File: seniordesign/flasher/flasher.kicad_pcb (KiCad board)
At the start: 2 copper layers, 17 parts, among them IC1 ATTINY24-SS, P1 PROG_PINS, P2 GPIO, P3 OUT, Q1 BC847S, Q2 BC847S

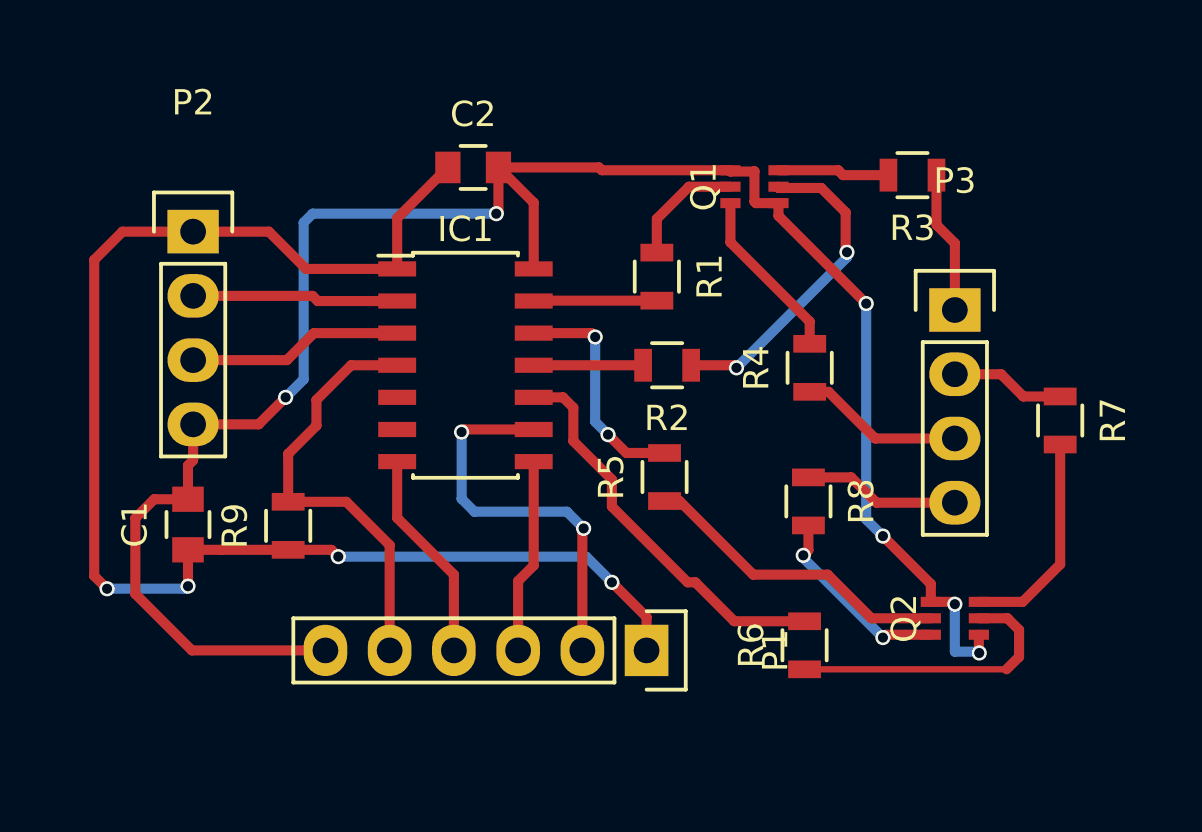
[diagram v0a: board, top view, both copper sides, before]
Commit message: Fix servo stuff, regenerate Gerber files for everything
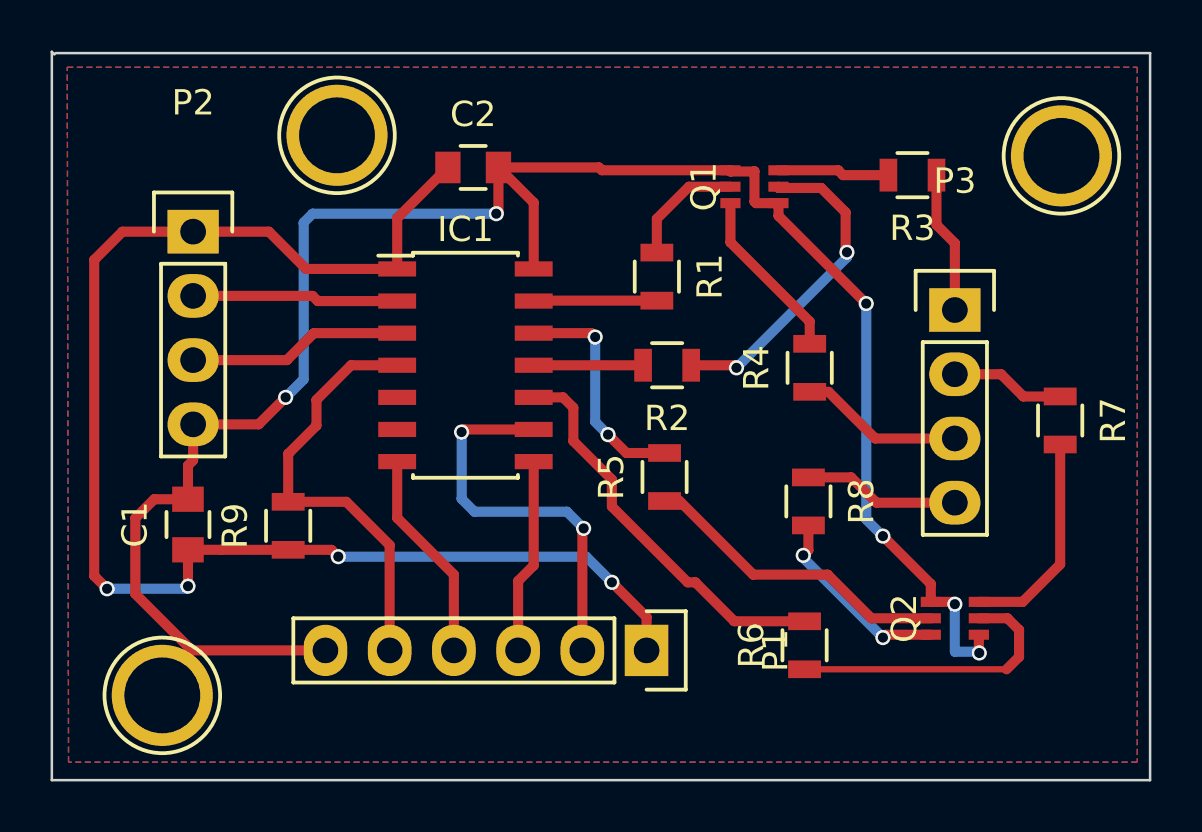
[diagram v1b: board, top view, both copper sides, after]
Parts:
- added REF**: 1pin, Connect:1pin, F.Cu at (144.3, 103.2)
- added REF**: 1pin, Connect:1pin, F.Cu at (179.9, 81.8)
- added REF**: 1pin, Connect:1pin, F.Cu at (151.2, 81.0)
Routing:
- added copper zone on B.Cu, net GND
- added copper zone on F.Cu, net GND
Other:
- board outline added: 43.4 x 28.8 mm
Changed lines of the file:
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@@
 (kicad_pcb (version 4) (host pcbnew "(2015-07-31 BZR 6030)-product")
   (general
-    (links 36)
+    (links 37)
     (no_connects 0)
-    (area 141.230399 78.611 183.183191 103.371801)
+    (area 139.903999 77.673999 183.438001 106.577601)
     (thickness 1.6)
-    (drawings 0)
+    (drawings 5)
     (tracks 175)
     (zones 0)
-    (modules 17)
+    (modules 20)
     (nets 27)
   )
@@
   )
   (setup
-    (last_trace_width 0.4)
+    (last_trace_width 0.25)
     (user_trace_width 0.4)
     (trace_clearance 0.2)
@@
     (mod_text_size 1 1)
     (mod_text_width 0.15)
-    (pad_size 1.5 1.5)
-    (pad_drill 0.6)
+    (pad_size 4 4)
+    (pad_drill 3)
     (pad_to_mask_clearance 0)
     (aux_axis_origin 0 0)
@@
       (outputformat 1)
       (mirror false)
-      (drillshape 1)
+      (drillshape 0)
       (scaleselection 1)
       (outputdirectory ""))
@@
     (add_net "Net-(Q2-Pad6)")
   )
+  (module Connect:1pin (layer F.Cu)
+    (at 144.3228 103.1748)
+    (descr "module 1 pin (ou trou mecanique de percage)")
+    (tags DEV)
+    (fp_text reference REF** (at 0 -3.048) (layer F.SilkS) hide
+      (effects (font (size 1 1) (thickness 0.15)))
+    )
+    (fp_text value 1pin (at 0 2.794) (layer F.Fab)
+      (effects (font (size 1 1) (thickness 0.15)))
+    )
+    (fp_circle (center 0 0) (end 0 -2.286) (layer F.SilkS) (width 0.15))
+    (pad 1 thru_hole circle (at 0 0) (size 4 4) (drill 3) (layers *.Cu *.Mask F.SilkS)
+      (net 2 GND))
+  )
+  (module Connect:1pin (layer F.Cu)
+    (at 179.8828 81.8388)
+    (descr "module 1 pin (ou trou mecanique de percage)")
+    (tags DEV)
+    (fp_text reference REF** (at 0 -3.048) (layer F.SilkS) hide
+      (effects (font (size 1 1) (thickness 0.15)))
+    )
+    (fp_text value 1pin (at 0 2.794) (layer F.Fab)
+      (effects (font (size 1 1) (thickness 0.15)))
+    )
+    (fp_circle (center 0 0) (end 0 -2.286) (layer F.SilkS) (width 0.15))
+    (pad 1 thru_hole circle (at 0 0) (size 4 4) (drill 3) (layers *.Cu *.Mask F.SilkS))
+  )
   (module Capacitors_SMD:C_0805 (layer F.Cu)
     (at 145.3388 96.4184 90)
@@
     )
   )
+  (module Connect:1pin (layer F.Cu)
+    (at 151.2316 81.026)
+    (descr "module 1 pin (ou trou mecanique de percage)")
+    (tags DEV)
+    (fp_text reference REF** (at 0 -3.048) (layer F.SilkS) hide
+      (effects (font (size 1 1) (thickness 0.15)))
+    )
+    (fp_text value 1pin (at 0 2.794) (layer F.Fab)
+      (effects (font (size 1 1) (thickness 0.15)))
+    )
+    (fp_circle (center 0 0) (end 0 -2.286) (layer F.SilkS) (width 0.15))
+    (pad 1 thru_hole circle (at 0 0) (size 4 4) (drill 3) (layers *.Cu *.Mask F.SilkS))
+  )
+  (gr_line (start 139.954 77.724) (end 140.0556 77.8256) (angle 90) (layer Edge.Cuts) (width 0.1))
+  (gr_line (start 139.954 106.5276) (end 139.954 77.724) (angle 90) (layer Edge.Cuts) (width 0.1))
+  (gr_line (start 183.388 106.5276) (end 139.954 106.5276) (angle 90) (layer Edge.Cuts) (width 0.1))
+  (gr_line (start 183.388 77.7748) (end 183.388 106.5276) (angle 90) (layer Edge.Cuts) (width 0.1))
+  (gr_line (start 140.1064 77.7748) (end 183.388 77.7748) (angle 90) (layer Edge.Cuts) (width 0.1))
   (segment (start 145.3388 97.4184) (end 145.3388 98.8568) (width 0.4) (layer F.Cu) (net 1))
   (segment (start 142.748 84.836) (end 145.542 84.836) (width 0.4) (layer F.Cu) (net 1))
@@
   (segment (start 159.0116 98.0364) (end 159.0116 93.9292) (width 0.4) (layer F.Cu) (net 9))
   (segment (start 158.3944 98.6536) (end 159.0116 98.0364) (width 0.4) (layer F.Cu) (net 9))
-  (segment (start 160.9344 101.3968) (end 160.9344 96.6216) (width 0.4) (layer F.Cu) (net 10) (status 400000))
-  (segment (start 156.2608 92.6592) (end 159.0116 92.6592) (width 0.4) (layer F.Cu) (net 10) (status 800000))
+  (segment (start 160.9344 101.3968) (end 160.9344 96.6216) (width 0.4) (layer F.Cu) (net 10))
+  (segment (start 156.2608 92.6592) (end 159.0116 92.6592) (width 0.4) (layer F.Cu) (net 10))
   (segment (start 156.1592 92.7608) (end 156.2608 92.6592) (width 0.4) (layer F.Cu) (net 10))
   (via (at 156.1592 92.7608) (size 0.6) (drill 0.4) (layers F.Cu B.Cu) (net 10))
@@
   (segment (start 172.3644 100.1268) (end 170.6372 98.3996) (width 0.4) (layer F.Cu) (net 23))
   (segment (start 164.78 95.4888) (end 164.1856 95.4888) (width 0.4) (layer F.Cu) (net 23))
-  (segment (start 174.7164 100.7768) (end 172.9336 100.7768) (width 0.4) (layer F.Cu) (net 24) (status 400000))
-  (segment (start 169.8752 97.4344) (end 169.8752 96.454) (width 0.4) (layer F.Cu) (net 24) (status 800000))
+  (segment (start 174.7164 100.7768) (end 172.9336 100.7768) (width 0.4) (layer F.Cu) (net 24))
+  (segment (start 169.8752 97.4344) (end 169.8752 96.454) (width 0.4) (layer F.Cu) (net 24))
   (segment (start 169.672 97.6376) (end 169.8752 97.4344) (width 0.4) (layer F.Cu) (net 24))
   (via (at 169.672 97.6376) (size 0.6) (drill 0.4) (layers F.Cu B.Cu) (net 24))
@@
   (segment (start 178.3484 99.4768) (end 179.832 97.9932) (width 0.4) (layer F.Cu) (net 26))
   (segment (start 179.832 97.9932) (end 179.832 93.2536) (width 0.4) (layer F.Cu) (net 26))
+  (zone (net 2) (net_name GND) (layer B.Cu) (hatch edge 0.508)
+    (connect_pads (clearance 0.508))
+    (min_thickness 0.254)
+    (fill yes (arc_segments 16) (thermal_gap 0.508) (thermal_bridge_width 0.508))
+    (polygon
+      (pts
+        (xy 140.5636 78.3336) (xy 182.88 78.3336) (xy 182.88 105.8164) (xy 140.6144 105.8164)
+      )
+    )
+  )
+  (zone (net 2) (net_name GND) (layer F.Cu) (hatch edge 0.508)
+    (connect_pads (clearance 0.508))
+    (min_thickness 0.254)
+    (fill yes (arc_segments 16) (thermal_gap 0.508) (thermal_bridge_width 0.508))
+    (polygon
+      (pts
+        (xy 140.5636 78.3336) (xy 182.88 78.3336) (xy 182.88 105.8164) (xy 140.6144 105.8164)
+      )
+    )
+  )
 )
